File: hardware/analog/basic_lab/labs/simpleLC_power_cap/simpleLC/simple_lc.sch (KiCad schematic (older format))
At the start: 8 parts, among them J1 Conn_01x04_Male, Q1 FQP27P06

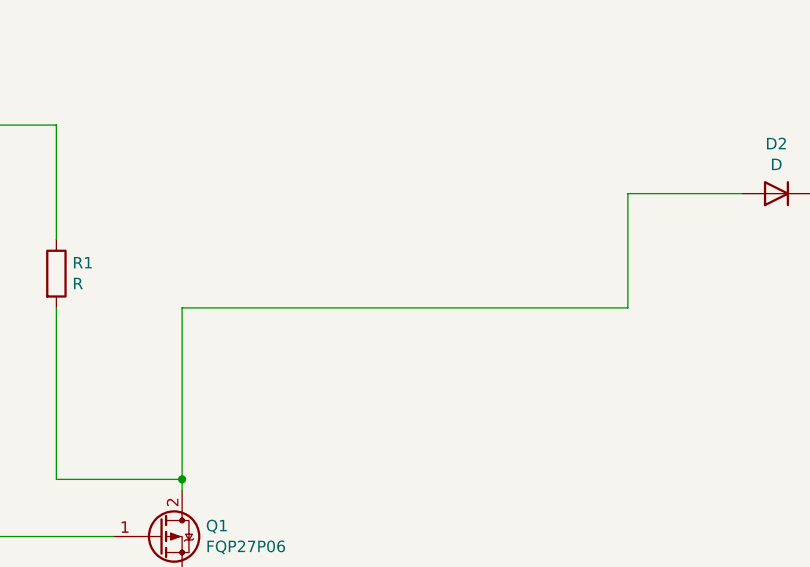
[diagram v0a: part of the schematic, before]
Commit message: preparation for the PWM-ADC cap detect
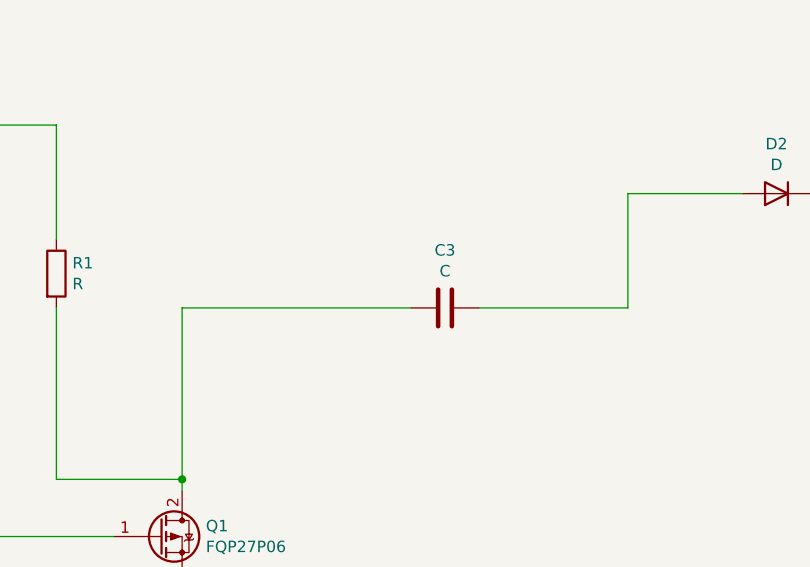
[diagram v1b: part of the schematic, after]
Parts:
- added C3: C, Capacitor_THT:C_Disc_D4.3mm_W1.9mm_P5.00mm, symbol Device:C
- C1: footprint Capacitor_THT:C_Disc_D3.8mm_W2.6mm_P2.50mm -> Capacitor_THT:C_Disc_D4.3mm_W1.9mm_P5.00mm
- C2: footprint (none) -> Capacitor_THT:C_Disc_D4.3mm_W1.9mm_P5.00mm
- D2: footprint (none) -> Diode_THT:D_DO-15_P10.16mm_Horizontal
- R1, R3: footprint (none) -> Resistor_THT:R_Axial_DIN0204_L3.6mm_D1.6mm_P5.08mm_Horizontal
- R2: footprint Resistor_THT:R_Axial_DIN0207_L6.3mm_D2.5mm_P2.54mm_Vertical -> Resistor_THT:R_Axial_DIN0204_L3.6mm_D1.6mm_P5.08mm_Horizontal
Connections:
- net at Q1.2 (D), R1.2: now also C3.1; no longer D2.2 (A)
- new net: C3.2, D2.2 (A)
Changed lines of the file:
@@
 F 0 "C1" H 1565 2546 50  0000 L CNN
 F 1 "C" H 1565 2455 50  0000 L CNN
-F 2 "Capacitor_THT:C_Disc_D3.8mm_W2.6mm_P2.50mm" H 1488 2350 50  0001 C CNN
+F 2 "Capacitor_THT:C_Disc_D4.3mm_W1.9mm_P5.00mm" H 1488 2350 50  0001 C CNN
 F 3 "~" H 1450 2500 50  0001 C CNN
 	1    1450 2500
@@
 F 0 "R2" H 3320 4346 50  0000 L CNN
 F 1 "R" H 3320 4255 50  0000 L CNN
-F 2 "Resistor_THT:R_Axial_DIN0207_L6.3mm_D2.5mm_P2.54mm_Vertical" V 3180 4300 50  0001 C CNN
+F 2 "Resistor_THT:R_Axial_DIN0204_L3.6mm_D1.6mm_P5.08mm_Horizontal" V 3180 4300 50  0001 C CNN
 F 3 "~" H 3250 4300 50  0001 C CNN
 	1    3250 4300
@@
 F 0 "R1" H 2770 2746 50  0000 L CNN
 F 1 "R" H 2770 2655 50  0000 L CNN
-F 2 "" V 2630 2700 50  0001 C CNN
+F 2 "Resistor_THT:R_Axial_DIN0204_L3.6mm_D1.6mm_P5.08mm_Horizontal" V 2630 2700 50  0001 C CNN
 F 3 "~" H 2700 2700 50  0001 C CNN
 	1    2700 2700
@@
 F 0 "D2" H 5850 2133 50  0000 C CNN
 F 1 "D" H 5850 2224 50  0000 C CNN
-F 2 "" H 5850 2350 50  0001 C CNN
+F 2 "Diode_THT:D_DO-15_P10.16mm_Horizontal" H 5850 2350 50  0001 C CNN
 F 3 "~" H 5850 2350 50  0001 C CNN
 	1    5850 2350
@@
 F 0 "C2" H 6565 2946 50  0000 L CNN
 F 1 "C" H 6565 2855 50  0000 L CNN
-F 2 "" H 6488 2750 50  0001 C CNN
+F 2 "Capacitor_THT:C_Disc_D4.3mm_W1.9mm_P5.00mm" H 6488 2750 50  0001 C CNN
 F 3 "~" H 6450 2900 50  0001 C CNN
 	1    6450 2900
@@
 F 0 "R3" H 7020 2946 50  0000 L CNN
 F 1 "R" H 7020 2855 50  0000 L CNN
-F 2 "" V 6880 2900 50  0001 C CNN
+F 2 "Resistor_THT:R_Axial_DIN0204_L3.6mm_D1.6mm_P5.08mm_Horizontal" V 6880 2900 50  0001 C CNN
 F 3 "~" H 6950 2900 50  0001 C CNN
 	1    6950 2900
@@
 Wire Wire Line
 	3250 2850 3250 3600
-Wire Wire Line
-	3250 2850 5200 2850
 Connection ~ 3250 3600
 Wire Wire Line
 	2700 2850 2700 3600
+$Comp
+L Device:C C3
+U 1 1 60CDE979
+P 4400 2850
+F 0 "C3" V 4652 2850 50  0000 C CNN
+F 1 "C" V 4561 2850 50  0000 C CNN
+F 2 "Capacitor_THT:C_Disc_D4.3mm_W1.9mm_P5.00mm" H 4438 2700 50  0001 C CNN
+F 3 "~" H 4400 2850 50  0001 C CNN
+	1    4400 2850
+	0    -1   -1   0
+$EndComp
+Wire Wire Line
+	3250 2850 4250 2850
+Wire Wire Line
+	4550 2850 5200 2850
 $EndSCHEMATC

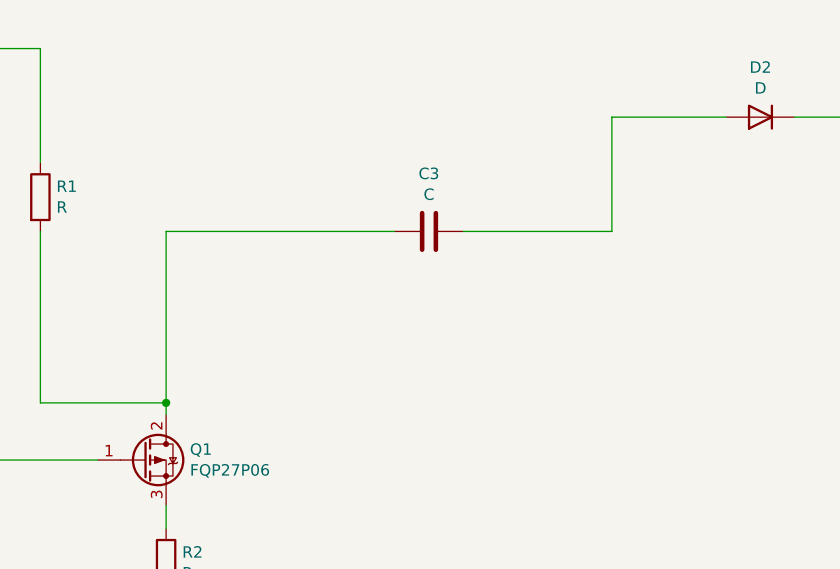
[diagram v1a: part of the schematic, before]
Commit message: preparation for the PWM-ADC pcbcap detect
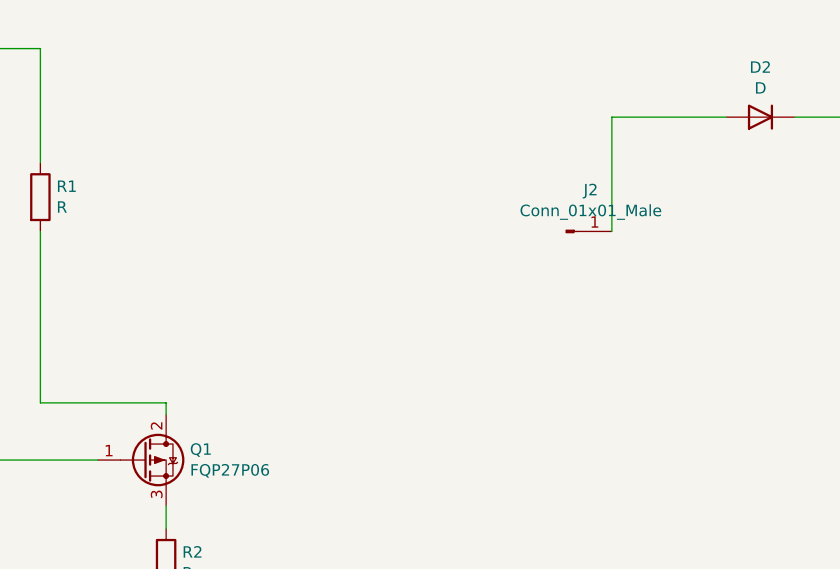
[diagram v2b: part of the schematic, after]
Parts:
- removed C3: C, Capacitor_THT:C_Disc_D4.3mm_W1.9mm_P5.00mm, symbol Device:C
- added J2: Conn_01x01_Male, Connector_PinHeader_2.54mm:PinHeader_1x01_P2.54mm_Vertical, symbol Connector:Conn_01x01_Male
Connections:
- net at D2.2 (A): now also J2.1 (Pin_1)
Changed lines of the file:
@@
 Connection ~ 6950 2350
-Wire Wire Line
-	3250 2850 3250 3600
-Connection ~ 3250 3600
 Wire Wire Line
 	2700 2850 2700 3600
 $Comp
-L Device:C C3
-U 1 1 60CDE979
-P 4400 2850
-F 0 "C3" V 4652 2850 50  0000 C CNN
-F 1 "C" V 4561 2850 50  0000 C CNN
-F 2 "Capacitor_THT:C_Disc_D4.3mm_W1.9mm_P5.00mm" H 4438 2700 50  0001 C CNN
-F 3 "~" H 4400 2850 50  0001 C CNN
-	1    4400 2850
-	0    -1   -1   0
+L Connector:Conn_01x01_Male J2
+U 1 1 60CE421D
+P 5000 2850
+F 0 "J2" H 5108 3031 50  0000 C CNN
+F 1 "Conn_01x01_Male" H 5108 2940 50  0000 C CNN
+F 2 "Connector_PinHeader_2.54mm:PinHeader_1x01_P2.54mm_Vertical" H 5000 2850 50  0001 C CNN
+F 3 "~" H 5000 2850 50  0001 C CNN
+	1    5000 2850
+	1    0    0    -1
 $EndComp
-Wire Wire Line
-	3250 2850 4250 2850
-Wire Wire Line
-	4550 2850 5200 2850
 $EndSCHEMATC
